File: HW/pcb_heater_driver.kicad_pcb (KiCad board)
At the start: 2 copper layers, 122.8 x 96 mm, 10 parts, among them Q1 BUK9M156-100EX, U1 ESP32-S2-MINI-2, U2 INA226

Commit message: Fixed board, big work in schematic, to finish
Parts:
- removed H8: MH2, MountingHole:MountingHole_3.2mm_M3_Pad_TopBottom
- added D1: SMBJ20A, Diode_THT:D_DO-201AE_P15.24mm_Horizontal, F.Cu at (98.0, 83.0)
- added D3: PRTR5V0U2X, Package_TO_SOT_SMD:SOT-143, F.Cu at (98.0, 98.0)
- added H6: AC_LIVE, MountingHole:MountingHole_2.2mm_M2_Pad_TopBottom, F.Cu at (98.9, 89.4)
- H1: value AC_LIVE -> MH2; footprint MountingHole:MountingHole_2.2mm_M2_Pad_TopBottom -> MountingHole:MountingHole_3.2mm_M3_Pad_TopBottom
- H2: value AC_NEUTRAL -> MH3; footprint MountingHole:MountingHole_2.2mm_M2_Pad_TopBottom -> MountingHole:MountingHole_3.2mm_M3_Pad_TopBottom
- H3: value AC_fixture -> MH2
- H4: value MH2 -> MH4
- H5: value MH3 -> AC_cable_fixture
- H7: value MH4 -> AC_NEUTRAL; footprint MountingHole:MountingHole_3.2mm_M3_Pad_TopBottom -> MountingHole:MountingHole_2.2mm_M2_Pad_TopBottom
- turned Q1 to 0 degrees
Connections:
- net Net-(C1-Pad1) renamed /Heater/mosfet_gate
- H1 pad 1: /LIVE -> unconnected-(H1-Pad1)
- H2 pad 1: /NEUTRAL -> unconnected-(H2-Pad1)
- H3 pad 1: (no net) -> unconnected-(H3-Pad1)
- H5 pad 1: unconnected-(H5-Pad1) -> (no net)
- H7 pad 1: unconnected-(H7-Pad1) -> /Power/NEUTRAL
- U1 pad 23: unconnected-(U1-Pad23) -> /MCU/USB_D-
- U1 pad 24: unconnected-(U1-Pad24) -> /MCU/USB_D+
- U1 pad 28: unconnected-(U1-Pad28) -> /MCU/SDA
- U1 pad 29: unconnected-(U1-Pad29) -> /MCU/SCL
- U1 pad 3: unconnected-(U1-Pad3) -> +3V3
- U1 pad 31: unconnected-(U1-Pad31) -> /MCU/Temp_mosfet
- U1 pad 32: unconnected-(U1-Pad32) -> /MCU/Temp_heater_3
- U1 pad 33: unconnected-(U1-Pad33) -> /MCU/Temp_heater_2
- U1 pad 34: unconnected-(U1-Pad34) -> /MCU/Temp_heater_1
- U1 pad 35: unconnected-(U1-Pad35) -> /MCU/TCK
- U1 pad 36: unconnected-(U1-Pad36) -> /MCU/TDO
- U1 pad 37: unconnected-(U1-Pad37) -> /MCU/TDI
- U1 pad 38: unconnected-(U1-Pad38) -> /MCU/TMS
- U1 pad 39: unconnected-(U1-Pad39) -> /MCU/TX
- U1 pad 40: unconnected-(U1-Pad40) -> /MCU/RX
- U1 pad 45: unconnected-(U1-Pad45) -> /MCU/RESET
- U1 pad 5: unconnected-(U1-Pad5) -> /MCU/current_sense_HIGH
- U1 pad 6: unconnected-(U1-Pad6) -> /MCU/current_sense_LOW

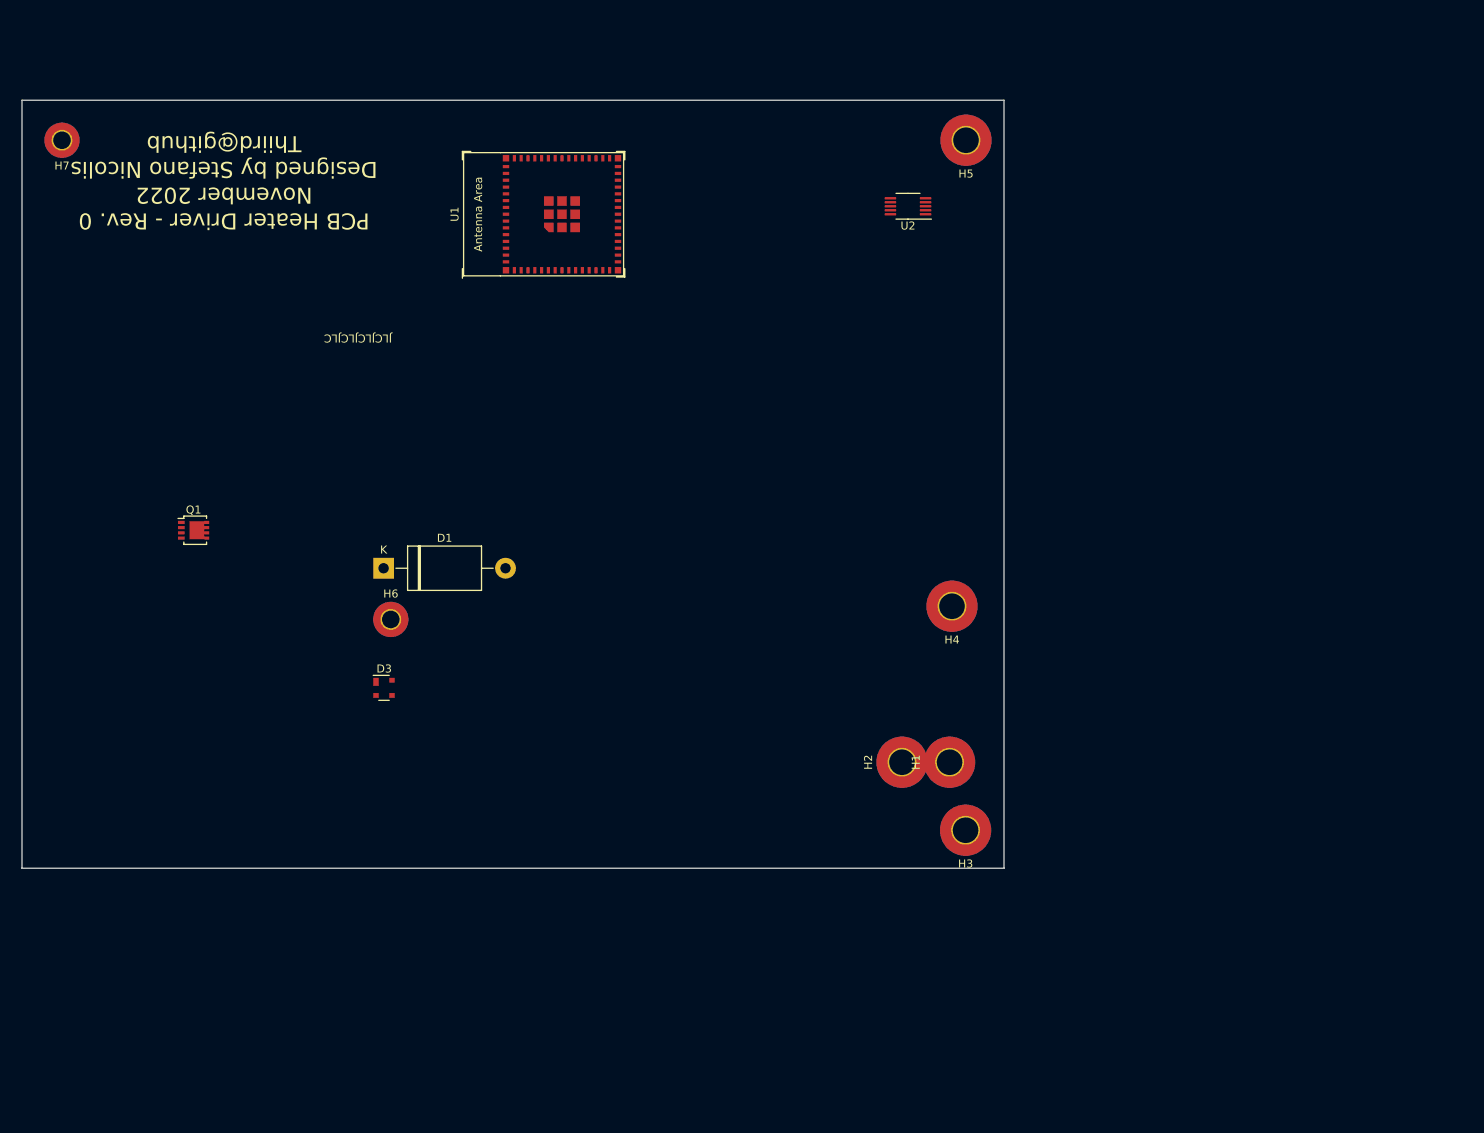
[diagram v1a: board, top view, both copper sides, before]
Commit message: Finished sch, to be checked. Initial components layout
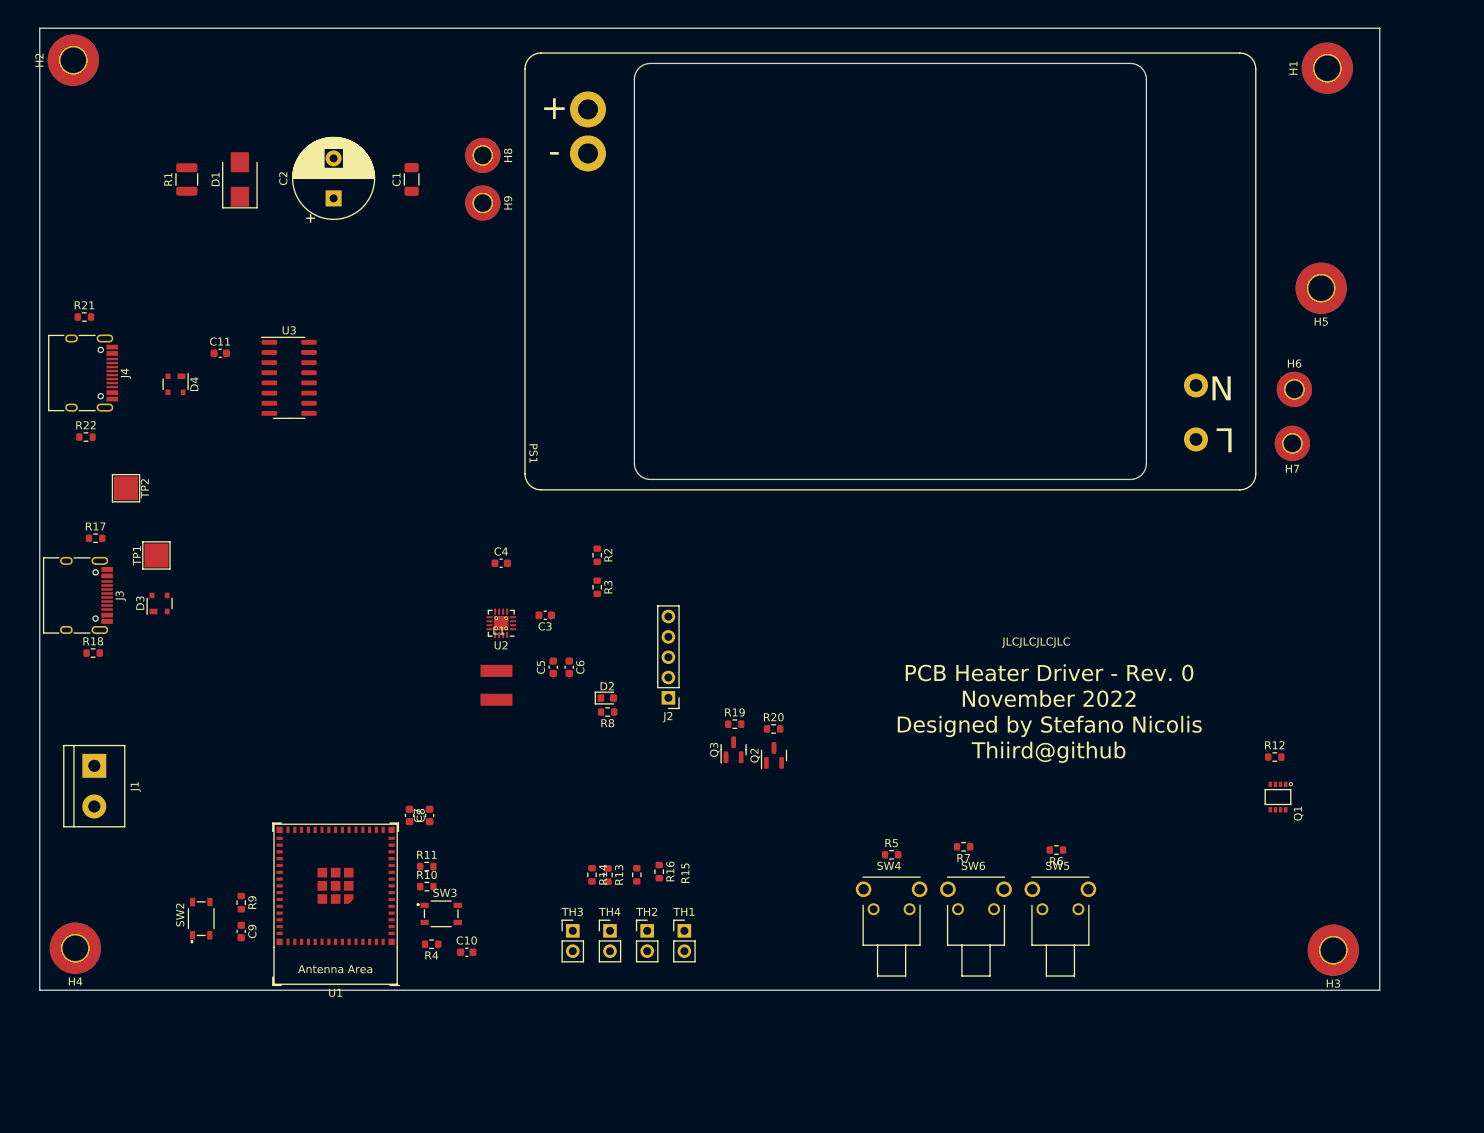
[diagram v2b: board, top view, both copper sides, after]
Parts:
- added C1: 1uF, Capacitor_SMD:C_1206_3216Metric, F.Cu at (101.5, 34.4)
- added C10: 1u, Capacitor_SMD:C_0603_1608Metric, F.Cu at (108.4, 131.0)
- added C11: 100n, Capacitor_SMD:C_0603_1608Metric, F.Cu at (77.6, 56.1)
- added C2: 200uF, Capacitor_THT:CP_Radial_D10.0mm_P5.00mm, F.Cu at (91.8, 36.8)
- added C3: 10uF, Capacitor_SMD:C_0603_1608Metric, F.Cu at (118.2, 88.9)
- added C4: 22nF, Capacitor_SMD:C_0603_1608Metric, F.Cu at (112.7, 82.4)
- added C5: 22u, Capacitor_SMD:C_0603_1608Metric, F.Cu at (119.2, 95.4)
- added C6: 22u, Capacitor_SMD:C_0603_1608Metric, F.Cu at (121.2, 95.4)
- added C7: 22uF, Capacitor_SMD:C_0603_1608Metric, F.Cu at (103.7, 113.9)
- added C8: 100n, Capacitor_SMD:C_0603_1608Metric, F.Cu at (101.2, 113.9)
- added C9: 1u, Capacitor_SMD:C_0603_1608Metric, F.Cu at (80.2, 128.4)
- added D2: RED, LED_SMD:LED_0603_1608Metric, F.Cu at (125.9, 99.2)
- added D4: PRTR5V0U2X, Package_TO_SOT_SMD:SOT-143, F.Cu at (72.0, 60.0)
- added H8: AC_LIVE, MountingHole:MountingHole_2.2mm_M2_Pad_TopBottom, F.Cu at (110.4, 31.4)
- added H9: AC_LIVE, MountingHole:MountingHole_2.2mm_M2_Pad_TopBottom, F.Cu at (110.4, 37.4)
- added J1: Heater, TerminalBlock:TerminalBlock_bornier-2_P5.08mm, F.Cu at (61.8, 107.7)
- added J2: JTAG, Connector_PinHeader_2.54mm:PinHeader_1x05_P2.54mm_Vertical, F.Cu at (133.6, 99.2)
- added J3: USB_C_Receptacle_USB2.0, Connector_USB:USB_C_Receptacle_HRO_TYPE-C-31-M-12, F.Cu at (59.4, 86.4)
- added J4: USB_C_Receptacle_USB2.0, Connector_USB:USB_C_Receptacle_HRO_TYPE-C-31-M-12, F.Cu at (60.0, 58.6)
- added L1: 4u7, BWVS005050404R7M00:BWVS005050404R7M00, F.Cu at (112.1, 97.2)
- added PS1: LD90-23B12R2, LD90-23B12R2:LD90-23B12R2, F.Cu at (161.3, 45.9)
- added Q2: BC817, Package_TO_SOT_SMD:SOT-23, F.Cu at (146.8, 106.4)
- added Q3: BC817, Package_TO_SOT_SMD:SOT-23, F.Cu at (141.8, 105.7)
- added R1: BR_DNP, Resistor_SMD:R_1210_3225Metric, F.Cu at (73.4, 34.4)
- added R10: 100k, Resistor_SMD:R_0603_1608Metric, F.Cu at (103.4, 122.8)
- added R11: TBD, Resistor_SMD:R_0603_1608Metric, F.Cu at (103.4, 120.3)
- added R12: 10k, Resistor_SMD:R_0603_1608Metric, F.Cu at (209.4, 106.6)
- added R13: 10k, Resistor_SMD:R_0603_1608Metric, F.Cu at (126.0, 121.3)
- added R14: 10k, Resistor_SMD:R_0603_1608Metric, F.Cu at (124.0, 121.3)
- added R15: 10k, Resistor_SMD:R_0603_1608Metric, F.Cu at (129.6, 121.3)
- added R16: 10k, Resistor_SMD:R_0603_1608Metric, F.Cu at (132.4, 120.9)
- added R17: 5k1, Resistor_SMD:R_0603_1608Metric, F.Cu at (62.0, 79.2)
- added R18: 5k1, Resistor_SMD:R_0603_1608Metric, F.Cu at (61.7, 93.6)
- added R19: 10k, Resistor_SMD:R_0603_1608Metric, F.Cu at (141.9, 102.5)
- added R2: 10k, Resistor_SMD:R_0603_1608Metric, F.Cu at (124.7, 81.4)
- added R20: 10k, Resistor_SMD:R_0603_1608Metric, F.Cu at (146.8, 103.1)
- added R21: 5k1, Resistor_SMD:R_0603_1608Metric, F.Cu at (60.6, 51.6)
- added R22: 5k1, Resistor_SMD:R_0603_1608Metric, F.Cu at (60.8, 66.6)
- added R3: 3750, Resistor_SMD:R_0603_1608Metric, F.Cu at (124.7, 85.4)
- added R4: 1k, Resistor_SMD:R_0603_1608Metric, F.Cu at (104.0, 130.0)
- added R5: 1k, Resistor_SMD:R_0603_1608Metric, F.Cu at (161.5, 118.8)
- added R6: 1k, Resistor_SMD:R_0603_1608Metric, F.Cu at (182.1, 118.2)
- added R7: 1k, Resistor_SMD:R_0603_1608Metric, F.Cu at (170.5, 117.8)
- added R8: 1k, Resistor_SMD:R_0603_1608Metric, F.Cu at (126.0, 101.0)
- added R9: 1k, Resistor_SMD:R_0603_1608Metric, F.Cu at (80.2, 124.8)
- added SW2: SW_DPST, SKRPACE010:SW_SKRPACE010, F.Cu at (75.2, 126.8)
- added SW3: SW_DPST, SKRPACE010:SW_SKRPACE010, F.Cu at (105.2, 126.2)
- added SW4: SW_SPST, 1-1825027-1:SW_1-1825027-1, F.Cu at (161.5, 125.6)
- added SW5: SW_SPST, 1-1825027-1:SW_1-1825027-1, F.Cu at (182.6, 125.6)
- added SW6: SW_SPST, 1-1825027-1:SW_1-1825027-1, F.Cu at (172.1, 125.6)
- added TH1: Heater_1, Connector_PinHeader_2.54mm:PinHeader_1x02_P2.54mm_Vertical, F.Cu at (135.6, 128.3)
- added TH2: Heater_2, Connector_PinHeader_2.54mm:PinHeader_1x02_P2.54mm_Vertical, F.Cu at (130.9, 128.3)
- added TH3: Heater_3, Connector_PinHeader_2.54mm:PinHeader_1x02_P2.54mm_Vertical, F.Cu at (121.6, 128.3)
- added TH4: mosfet, Connector_PinHeader_2.54mm:PinHeader_1x02_P2.54mm_Vertical, F.Cu at (126.3, 128.3)
- added TP1: TestPoint, TestPoint:TestPoint_Pad_3.0x3.0mm, F.Cu at (69.6, 81.4)
- added TP2: TestPoint, TestPoint:TestPoint_Pad_3.0x3.0mm, F.Cu at (65.8, 73.0)
- added U3: CH340C, Package_SO:SOIC-16_3.9x9.9mm_P1.27mm, F.Cu at (86.2, 59.2)
- D1: footprint Diode_THT:D_DO-201AE_P15.24mm_Horizontal -> Diode_SMD:D_SMB
- Q1: value BUK9M156-100EX -> RQ3E110AJ; footprint Package_TO_SOT_SMD:LFPAK33 -> SOTFL65P330X80-8N:SOTFL65P330X80-8N
- U2: value INA226 -> TS30042-M000QFNR; footprint Package_SO:VSSOP-10_3x3mm_P0.5mm -> Package_DFN_QFN:QFN-16-1EP_3x3mm_P0.5mm_EP1.75x1.75mm_ThermalVias
- moved H7 158.4 mm to (211.6, 67.4)
- moved Q1 139.6 mm to (209.8, 111.6), turned to -90 degrees
- moved H2 135.8 mm to (59.2, 19.5)
- moved H4 117.6 mm to (59.5, 130.5)
- moved H6 116.6 mm to (211.8, 60.6)
- moved H1 98.8 mm to (216.0, 20.5)
- moved U1 88.6 mm to (92.0, 122.7), turned to 180 degrees
- moved U2 72.8 mm to (112.7, 89.9)
- moved D1 51.8 mm to (80.0, 34.4), turned to 90 degrees
- moved H3 48.4 mm to (216.7, 130.8)
- moved H5 48.1 mm to (215.2, 48.0)
- moved D3 30.0 mm to (70.0, 87.4), turned to 90 degrees
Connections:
- net /MCU/SCL renamed SCL
- net /MCU/SDA renamed SDA
- net /MCU/USB_D+ renamed USB_D+
- net /MCU/USB_D- renamed USB_D-
- Q1 pad 2: GND -> mosfet_gate
- Q1 pad 3: GND -> heater_LOW
- U1 pad 15: unconnected-(U1-Pad15) -> /MCU/Temp_heater_1
- U1 pad 16: unconnected-(U1-Pad16) -> /MCU/Temp_heater_2
- U1 pad 17: unconnected-(U1-Pad17) -> /MCU/Temp_heater_3
- U1 pad 18: unconnected-(U1-Pad18) -> /MCU/Temp_mosfet
- U1 pad 31: /MCU/Temp_mosfet -> unconnected-(U1-Pad31)
- U1 pad 32: /MCU/Temp_heater_3 -> unconnected-(U1-Pad32)
- U1 pad 33: /MCU/Temp_heater_2 -> unconnected-(U1-Pad33)
- U1 pad 34: /MCU/Temp_heater_1 -> unconnected-(U1-Pad34)
- U1 pad 39: /MCU/TX -> TX
- U1 pad 4: unconnected-(U1-Pad4) -> /MCU/BOOT0
- U1 pad 40: /MCU/RX -> RX
- U1 pad 5: /MCU/current_sense_HIGH -> unconnected-(U1-Pad5)
- U1 pad 6: /MCU/current_sense_LOW -> current_sense_LOW
- U2 pad 1: unconnected-(U2-Pad1) -> Net-(C4-Pad2)
- U2 pad 10: unconnected-(U2-Pad10) -> Net-(C4-Pad1)
- U2 pad 2: unconnected-(U2-Pad2) -> +12V
- U2 pad 3: unconnected-(U2-Pad3) -> +12V
- U2 pad 4: unconnected-(U2-Pad4) -> GND
- U2 pad 5: unconnected-(U2-Pad5) -> Net-(R2-Pad2)
- U2 pad 6: unconnected-(U2-Pad6) -> GND
- U2 pad 7: unconnected-(U2-Pad7) -> GND
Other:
- board size 122.8 x 96 mm -> 167.5 x 120.2 mm

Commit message: Sch finalized, added EMC stuff, user buttons and oled
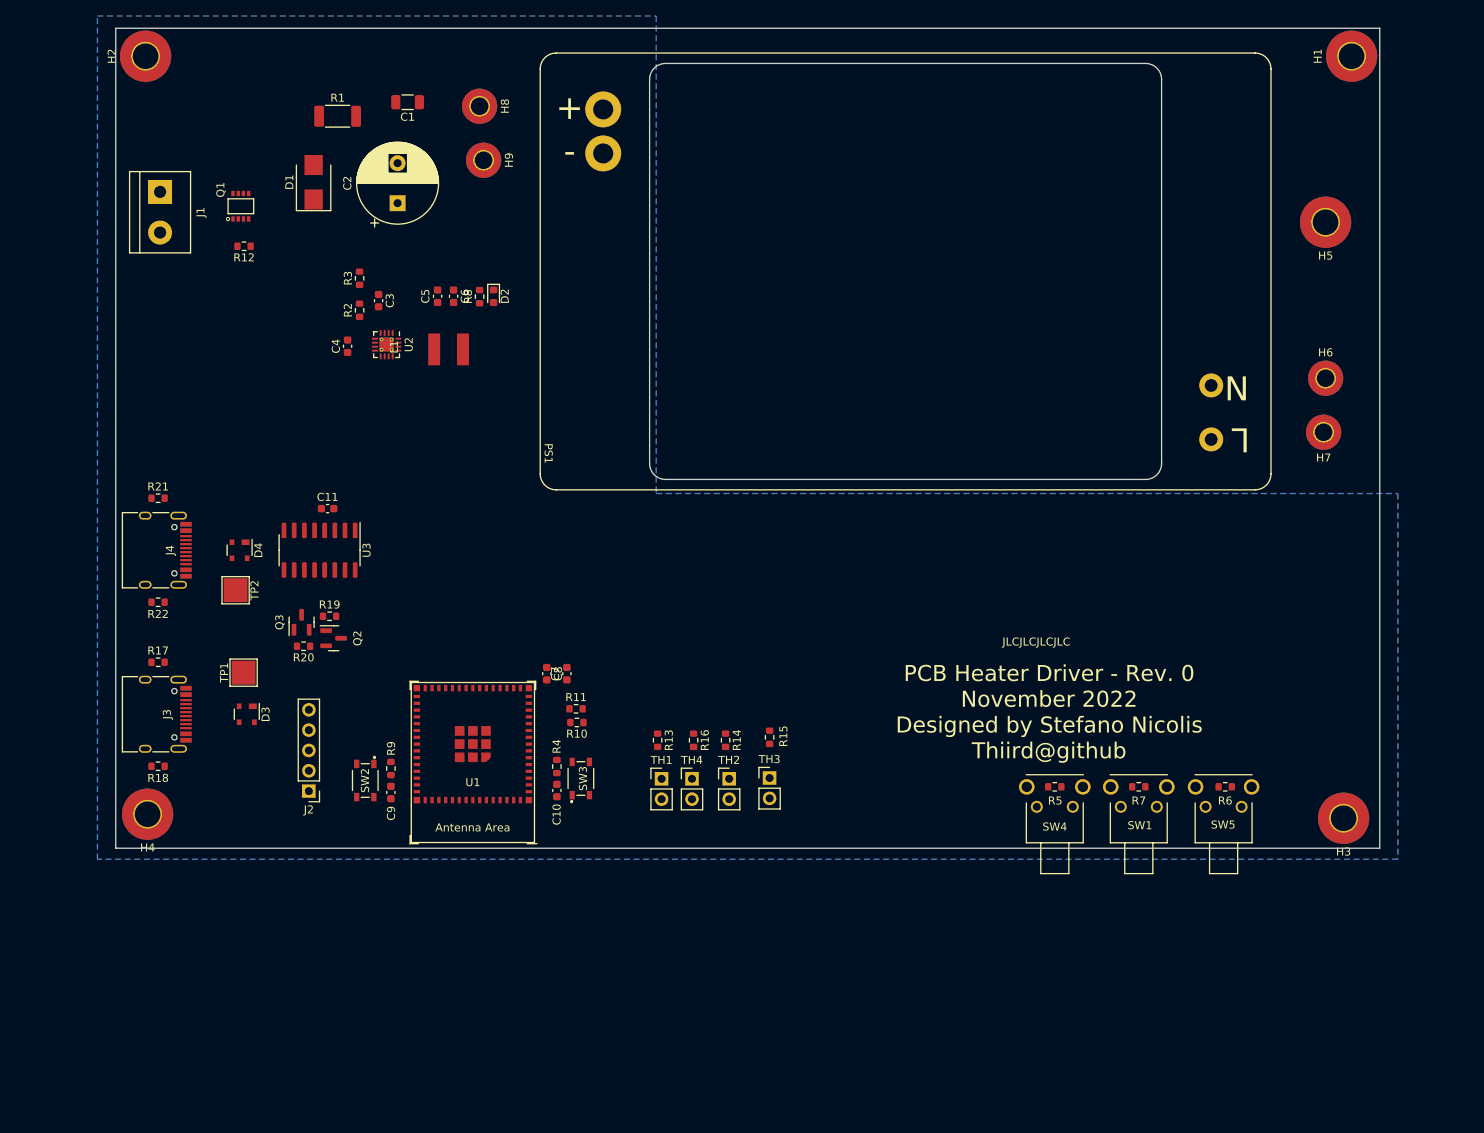
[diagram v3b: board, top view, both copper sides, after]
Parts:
- removed SW6: SW_SPST, 1-1825027-1:SW_1-1825027-1
- added SW1: SW_SPST, 1-1825027-1:SW_1-1825027-1, F.Cu at (192.4, 112.8)
- C1: value 1uF -> 1u
- R1: footprint Resistor_SMD:R_1210_3225Metric -> Resistor_SMD:R_2010_5025Metric
- moved Q1 149.2 mm to (80.2, 37.8), turned to 90 degrees
- moved R12 143.8 mm to (80.6, 42.8), turned to 180 degrees
- moved J1 72.2 mm to (70.1, 36.0)
- moved R20 59.7 mm to (88.0, 92.8), turned to 180 degrees
- moved Q2 57.0 mm to (91.8, 91.8), turned to 0 degrees
- moved Q3 56.3 mm to (87.8, 89.8)
- moved R8 54.3 mm to (110.0, 49.1), turned to 90 degrees
- moved R19 52.4 mm to (91.2, 89.0)
- moved D2 52.2 mm to (111.8, 49.0), turned to -90 degrees
- moved R3 48.7 mm to (95.0, 46.8), turned to 90 degrees
- moved C6 48.6 mm to (106.8, 49.0)
- moved C5 48.6 mm to (104.8, 49.0)
- moved J2 46.4 mm to (88.7, 110.9)
- moved C3 44.5 mm to (97.4, 49.6), turned to -90 degrees
- moved R2 42.7 mm to (95.0, 50.7), turned to 90 degrees
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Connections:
- net /Power/NEUTRAL renamed Net-(PS1-Pad1)
- C10 pad 1: /MCU/BOOT0 -> GPIO0
- C9 pad 1: /MCU/RESET -> RESET
- H6 pad 1: /Power/LIVE -> Net-(H6-Pad1)
- PS1 pad 2: /Power/LIVE -> Net-(PS1-Pad2)
- R4 pad 2: /MCU/BOOT0 -> GPIO0
- R9 pad 2: /MCU/RESET -> RESET
- SW2 pad 1: /MCU/RESET -> RESET
- SW2 pad 2: /MCU/RESET -> RESET
- SW3 pad 1: /MCU/BOOT0 -> GPIO0
- SW3 pad 2: /MCU/BOOT0 -> GPIO0
- SW4 pad 1: /MCU/temperature_plus -> temperature_minus
- SW4 pad 2: Net-(R5-Pad1) -> Net-(R6-Pad1)
- SW5 pad 1: /MCU/temperature_minus -> user_action
- SW5 pad 2: Net-(R6-Pad1) -> Net-(R7-Pad1)
- U1 pad 14: unconnected-(U1-Pad14) -> temp_heater_1
- U1 pad 15: /MCU/Temp_heater_1 -> temp_heater_2
- U1 pad 16: /MCU/Temp_heater_2 -> temp_heater_3
- U1 pad 17: /MCU/Temp_heater_3 -> temp_mosfet
- U1 pad 18: /MCU/Temp_mosfet -> unconnected-(U1-Pad18)
- U1 pad 32: unconnected-(U1-Pad32) -> user_action
- U1 pad 33: unconnected-(U1-Pad33) -> temperature_minus
- U1 pad 34: unconnected-(U1-Pad34) -> temperature_plus
- U1 pad 4: /MCU/BOOT0 -> GPIO0
- U1 pad 45: /MCU/RESET -> RESET
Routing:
- added copper zone on B.Cu, net GND
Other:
- board size 167.5 x 120.2 mm -> 158 x 102.5 mm
